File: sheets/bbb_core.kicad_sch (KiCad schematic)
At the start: 11 parts, among them P10 BeagleBone_Black_Header, P11 BeagleBone_Black_Header, SW2 SW_DIP_x02, U2 CAT24C256

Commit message: push
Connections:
- net GPIO117 renamed SPI0.CS3
- net GPIO2 renamed SPI0.SCLK
- net GPIO3 renamed SPI0.D0
- net GPIO4 renamed SPI0.CS0
- net GPIO48 renamed SPI0.CS1
- net GPIO49 renamed SPI0.CS2
- net GPIO5 renamed SPI0.D1

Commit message: pushing storage
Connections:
- net GPIO65 renamed MMC1.RST
- net MMC1.DAT3 renamed MCC1.DAT3
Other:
- moved on the sheet: P11

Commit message: push
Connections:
- net GPIO122 renamed SPI1.D1
- net GPIO14 renamed UART1_RXD
- net GPIO15 renamed UART1_TXD
- net GPIO26 renamed SPI1.CS8
- net GPIO44 renamed SPI1.CS7
- net GPIO45 renamed SPI1.CS3
- net GPIO47 renamed SPI1.CS4
- net GPIO66 renamed SPI1.CS1
- net GPIO67 renamed SPI1.CS5
- net GPIO68 renamed SPI1.CS6
- net GPIO69 renamed SPI1.CS2

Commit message: allocating pins ?
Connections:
- net GPIO22 renamed ACDS_GPIO_3
- net GPIO23 renamed ACDS_PWM_3
- net GPIO27 renamed ACDS_GPIO_2
- net GPIO40 renamed ACDS_PWM_1
- net GPIO51 renamed ACDS_PWM_2
- net GPIO60 renamed ACDS_GPIO_1
- net GPIO7 renamed HEATER_PWM
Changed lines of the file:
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@@
-		)
-	)
-	(label "GPIO27"
-		(at 187.96 53.34 0)
-		(effects
-			(font
-				(size 1.27 1.27)
-			)
-			(justify left bottom)
 		)
 	)
@@
 		)
 	)
-	(label "I2C2.SDA"
-		(at 135.89 55.88 180)
-		(effects
-			(font
-				(size 1.27 1.27)
-			)
-			(justify right bottom)
-		)
-	)
 	(label "LCD.DATA8"
 		(at 187.96 78.74 0)
@@
 		)
 	)
-	(label "GPIO51"
-		(at 135.89 50.8 180)
-		(effects
-			(font
-				(size 1.27 1.27)
-			)
-			(justify right bottom)
-		)
-	)
 	(label "LCD.AC_BIAS_E"
 		(at 238.76 68.58 180)
@@
 		)
 	)
-	(label "GPIO40"
-		(at 135.89 48.26 180)
-		(effects
-			(font
-				(size 1.27 1.27)
-			)
-			(justify right bottom)
-		)
-	)
 	(label "PWR_BUT"
 		(at 85.09 43.18 0)
@@
 		)
 	)
-	(label "GPIO60"
-		(at 135.89 45.72 180)
-		(effects
-			(font
-				(size 1.27 1.27)
-			)
-			(justify right bottom)
-		)
-	)
 	(label "I2C2.SDA"
 		(at 161.29 119.38 180)
@@
 			)
 			(justify right bottom)
-		)
-	)
-	(label "GPIO23"
-		(at 187.96 48.26 0)
-		(effects
-			(font
-				(size 1.27 1.27)
-			)
-			(justify left bottom)
-		)
-	)
-	(label "GPIO7"
-		(at 135.89 83.82 180)
-		(effects
-			(font
-				(size 1.27 1.27)
-			)
-			(justify right bottom)
-		)
-	)
-	(label "I2C2.SCL"
-		(at 85.09 55.88 0)
-		(effects
-			(font
-				(size 1.27 1.27)
-			)
-			(justify left bottom)
-		)
-	)
-	(label "GPIO22"
-		(at 187.96 55.88 0)
-		(effects
-			(font
-				(size 1.27 1.27)
-			)
-			(justify left bottom)
 		)
 	)
@@
 		)
 	)
+	(global_label "HEATER_PWM"
+		(shape output)
+		(at 135.89 83.82 0)
+		(fields_autoplaced yes)
+		(effects
+			(font
+				(size 1.27 1.27)
+			)
+			(justify left)
+		)
+		(property "Intersheetrefs" "${INTERSHEET_REFS}"
+			(at 151.0654 83.82 0)
+			(hide yes)
+			(show_name no)
+			(do_not_autoplace no)
+			(effects
+				(font
+					(size 1.27 1.27)
+				)
+				(justify left)
+			)
+		)
+	)
+	(global_label "ACDS_PWM_1"
+		(shape output)
+		(at 135.89 48.26 0)
+		(fields_autoplaced yes)
+		(effects
+			(font
+				(size 1.27 1.27)
+			)
+			(justify left)
+		)
+		(property "Intersheetrefs" "${INTERSHEET_REFS}"
+			(at 151.1259 48.26 0)
+			(hide yes)
+			(show_name no)
+			(do_not_autoplace no)
+			(effects
+				(font
+					(size 1.27 1.27)
+				)
+				(justify left)
+			)
+		)
+	)
 	(global_label "SPI1.D1"
 		(shape output)
@@
 		)
 	)
+	(global_label "ACDS_GPIO_2"
+		(shape output)
+		(at 187.96 53.34 180)
+		(fields_autoplaced yes)
+		(effects
+			(font
+				(size 1.27 1.27)
+			)
+			(justify right)
+		)
+		(property "Intersheetrefs" "${INTERSHEET_REFS}"
+			(at 172.4216 53.34 0)
+			(hide yes)
+			(show_name no)
+			(do_not_autoplace no)
+			(effects
+				(font
+					(size 1.27 1.27)
+				)
+				(justify right)
+			)
+		)
+	)
 	(global_label "SPI1.CS7"
 		(shape output)
@@
 		(property "Intersheetrefs" "${INTERSHEET_REFS}"
 			(at 250.4279 45.72 0)
+			(hide yes)
+			(show_name no)
+			(do_not_autoplace no)
+			(effects
+				(font
+					(size 1.27 1.27)
+				)
+				(justify left)
+			)
+		)
+	)
+	(global_label "ACDS_GPIO_1"
+		(shape output)
+		(at 135.89 45.72 0)
+		(fields_autoplaced yes)
+		(effects
+			(font
+				(size 1.27 1.27)
+			)
+			(justify left)
+		)
+		(property "Intersheetrefs" "${INTERSHEET_REFS}"
+			(at 151.4284 45.72 0)
 			(hide yes)
 			(show_name no)
@@
 		)
 	)
+	(global_label "ACDS_GPIO_3"
+		(shape output)
+		(at 187.96 55.88 180)
+		(fields_autoplaced yes)
+		(effects
+			(font
+				(size 1.27 1.27)
+			)
+			(justify right)
+		)
+		(property "Intersheetrefs" "${INTERSHEET_REFS}"
+			(at 172.4216 55.88 0)
+			(hide yes)
+			(show_name no)
+			(do_not_autoplace no)
+			(effects
+				(font
+					(size 1.27 1.27)
+				)
+				(justify right)
+			)
+		)
+	)
 	(global_label "SPI1.CS0"
 		(shape output)
@@
 		)
 	)
+	(global_label "ACDS_PWM_2"
+		(shape output)
+		(at 135.89 50.8 0)
+		(fields_autoplaced yes)
+		(effects
+			(font
+				(size 1.27 1.27)
+			)
+			(justify left)
+		)
+		(property "Intersheetrefs" "${INTERSHEET_REFS}"
+			(at 151.1259 50.8 0)
+			(hide yes)
+			(show_name no)
+			(do_not_autoplace no)
+			(effects
+				(font
+					(size 1.27 1.27)
+				)
+				(justify left)
+			)
+		)
+	)
 	(global_label "MMC1.CLK"
 		(shape output)
@@
 		)
 	)
+	(global_label "ACDS_PWM_3"
+		(shape output)
+		(at 187.96 48.26 180)
+		(fields_autoplaced yes)
+		(effects
+			(font
+				(size 1.27 1.27)
+			)
+			(justify right)
+		)
+		(property "Intersheetrefs" "${INTERSHEET_REFS}"
+			(at 172.7241 48.26 0)
+			(hide yes)
+			(show_name no)
+			(do_not_autoplace no)
+			(effects
+				(font
+					(size 1.27 1.27)
+				)
+				(justify right)
+			)
+		)
+	)
 	(global_label "SPI0.CS1"
 		(shape output)
@@
 			)
 		)
+	)
+	(global_label "I2C2.SCL"
+		(shape output)
+		(at 85.09 55.88 180)
+		(fields_autoplaced yes)
+		(effects
+			(font
+				(size 1.27 1.27)
+			)
+			(justify right)
+		)
+		(property "Intersheetrefs" "${INTERSHEET_REFS}"
+			(at 73.6035 55.88 0)
+			(hide yes)
+			(show_name no)
+			(do_not_autoplace no)
+			(effects
+				(font
+					(size 1.27 1.27)
+				)
+				(justify right)
+			)
+		)
+	)
+	(global_label "I2C2.SDA"
+		(shape output)
+		(at 135.89 55.88 0)
+		(fields_autoplaced yes)
+		(effects
+			(font
+				(size 1.27 1.27)
+			)
+			(justify left)
+		)
+		(property "Intersheetrefs" "${INTERSHEET_REFS}"
+			(at 147.437 55.88 0)
+			(hide yes)
+			(show_name no)
+			(do_not_autoplace no)
+			(effects
+				(font
+					(size 1.27 1.27)
+				)
+				(justify left)
+			)
+		)

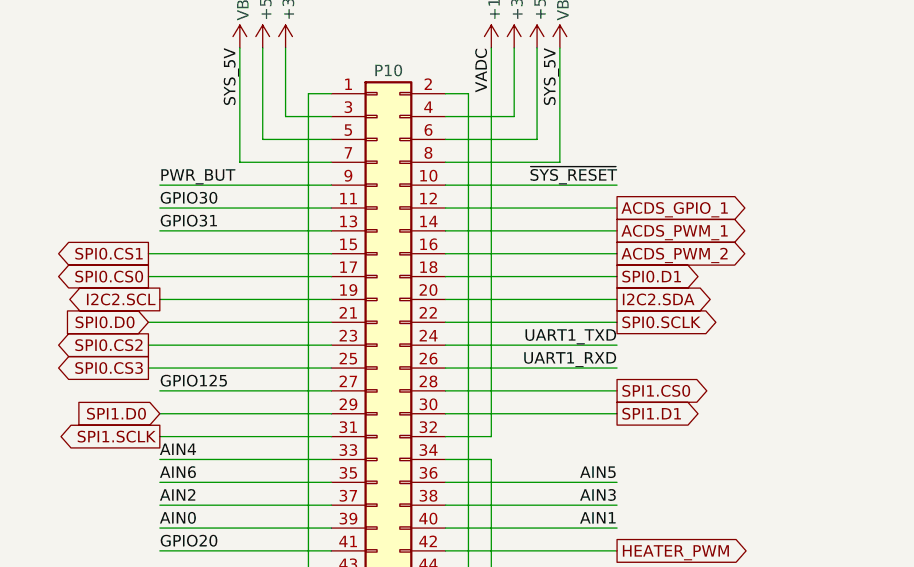
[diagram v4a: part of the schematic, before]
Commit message: uart global labels (not mapped onto pc104 yet)
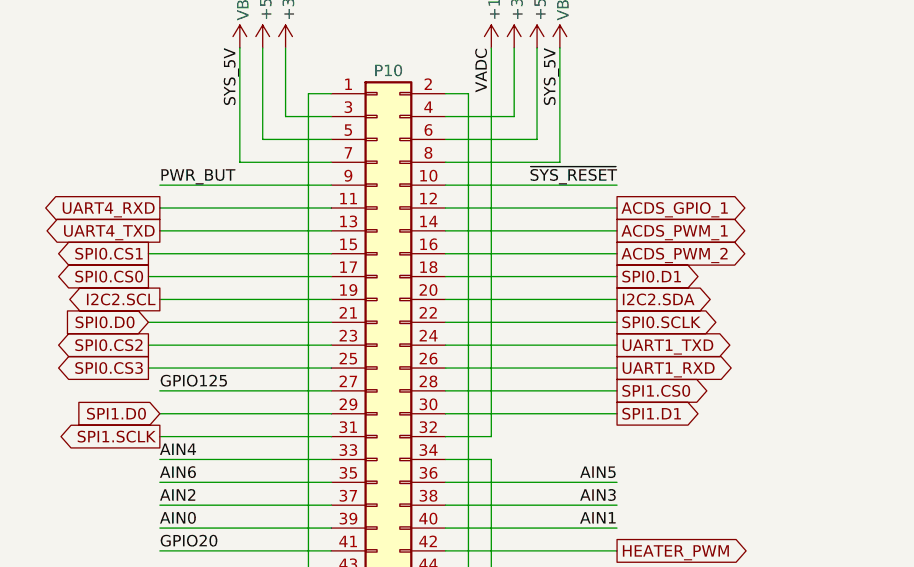
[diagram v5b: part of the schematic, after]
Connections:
- net GPIO30 renamed UART4_RXD
- net GPIO31 renamed UART4_TXD
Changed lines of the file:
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@@
-		)
-	)
-	(label "GPIO30"
-		(at 85.09 45.72 0)
-		(effects
-			(font
-				(size 1.27 1.27)
-			)
-			(justify left bottom)
 		)
 	)
@@
 		)
 	)
-	(label "GPIO31"
-		(at 85.09 48.26 0)
-		(effects
-			(font
-				(size 1.27 1.27)
-			)
-			(justify left bottom)
-		)
-	)
-	(label "UART1_RXD"
-		(at 135.89 63.5 180)
-		(effects
-			(font
-				(size 1.27 1.27)
-			)
-			(justify right bottom)
-		)
-	)
 	(label "GPIO61"
 		(at 238.76 66.04 180)
@@
 	(label "LCD.DATA5"
 		(at 238.76 83.82 180)
-		(effects
-			(font
-				(size 1.27 1.27)
-			)
-			(justify right bottom)
-		)
-	)
-	(label "UART1_TXD"
-		(at 135.89 60.96 180)
 		(effects
 			(font
@@
 		)
 	)
+	(global_label "UART4_RXD"
+		(shape output)
+		(at 85.09 45.72 180)
+		(fields_autoplaced yes)
+		(effects
+			(font
+				(size 1.27 1.27)
+			)
+			(justify right)
+		)
+		(property "Intersheetrefs" "${INTERSHEET_REFS}"
+			(at 71.4264 45.72 0)
+			(hide yes)
+			(show_name no)
+			(do_not_autoplace no)
+			(effects
+				(font
+					(size 1.27 1.27)
+				)
+				(justify right)
+			)
+		)
+	)
 	(global_label "SPI1.CS2"
 		(shape output)
@@
 		(property "Intersheetrefs" "${INTERSHEET_REFS}"
 			(at 176.2921 40.64 0)
+			(hide yes)
+			(show_name no)
+			(do_not_autoplace no)
+			(effects
+				(font
+					(size 1.27 1.27)
+				)
+				(justify right)
+			)
+		)
+	)
+	(global_label "UART4_TXD"
+		(shape output)
+		(at 85.09 48.26 180)
+		(fields_autoplaced yes)
+		(effects
+			(font
+				(size 1.27 1.27)
+			)
+			(justify right)
+		)
+		(property "Intersheetrefs" "${INTERSHEET_REFS}"
+			(at 71.7288 48.26 0)
 			(hide yes)
 			(show_name no)
@@
 			(hide yes)
 			(show_name no)
+			(do_not_autoplace no)
+			(effects
+				(font
+					(size 1.27 1.27)
+				)
+				(justify left)
+			)
+		)
+	)
+	(global_label "UART1_TXD"
+		(shape output)
+		(at 135.89 60.96 0)
+		(fields_autoplaced yes)
+		(effects
+			(font
+				(size 1.27 1.27)
+			)
+			(justify left)
+		)
+		(property "Intersheetrefs" "${INTERSHEET_REFS}"
+			(at 149.2512 60.96 0)
+			(hide yes)
+			(show_name no)
+			(do_not_autoplace no)
+			(effects
+				(font
+					(size 1.27 1.27)
+				)
+				(justify left)
+			)
+		)
+	)
+	(global_label "UART1_RXD"
+		(shape output)
+		(at 135.89 63.5 0)
+		(fields_autoplaced yes)
+		(effects
+			(font
+				(size 1.27 1.27)
+			)
+			(justify left)
+		)
+		(property "Intersheetrefs" "${INTERSHEET_REFS}"
+			(at 149.5536 63.5 0)
+			(hide yes)
+			(show_name no)

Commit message: one more uart (I think it is needed)
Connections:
- net LCD.DATA9 is gone; now on net UART1_RXD: P11.38 (Pin_38)
- net LCD.DATA8 renamed UART5_TXD
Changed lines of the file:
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@@
-		)
-	)
-	(label "LCD.DATA8"
-		(at 187.96 78.74 0)
-		(effects
-			(font
-				(size 1.27 1.27)
-			)
-			(justify left bottom)
 		)
 	)
@@
 	(label "AIN3"
 		(at 135.89 78.74 180)
-		(effects
-			(font
-				(size 1.27 1.27)
-			)
-			(justify right bottom)
-		)
-	)
-	(label "LCD.DATA9"
-		(at 238.76 78.74 180)
 		(effects
 			(font
@@
 	)
 	(global_label "UART4_RXD"
-		(shape output)
+		(shape input)
 		(at 85.09 45.72 180)
 		(fields_autoplaced yes)
@@
 		)
 	)
+	(global_label "UART1_RXD"
+		(shape input)
+		(at 238.76 78.74 0)
+		(fields_autoplaced yes)
+		(effects
+			(font
+				(size 1.27 1.27)
+			)
+			(justify left)
+		)
+		(property "Intersheetrefs" "${INTERSHEET_REFS}"
+			(at 252.4236 78.74 0)
+			(hide yes)
+			(show_name no)
+			(do_not_autoplace no)
+			(effects
+				(font
+					(size 1.27 1.27)
+				)
+				(justify left)
+			)
+		)
+	)
 	(global_label "UART1_TXD"
 		(shape output)
@@
 		)
 	)
+	(global_label "UART5_TXD"
+		(shape output)
+		(at 187.96 78.74 180)
+		(fields_autoplaced yes)
+		(effects
+			(font
+				(size 1.27 1.27)
+			)
+			(justify right)
+		)
+		(property "Intersheetrefs" "${INTERSHEET_REFS}"
+			(at 174.5988 78.74 0)
+			(hide yes)
+			(show_name no)
+			(do_not_autoplace no)
+			(effects
+				(font
+					(size 1.27 1.27)
+				)
+				(justify right)
+			)
+		)
+	)
 	(global_label "UART1_RXD"
-		(shape output)
+		(shape input)
 		(at 135.89 63.5 0)
 		(fields_autoplaced yes)

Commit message: Update bbb_core.kicad_sch
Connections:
- net UART1_RXD: no longer P11.38 (Pin_38)
- new net UART5_RXD: P11.38 (Pin_38)
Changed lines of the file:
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@@
 		)
 	)
-	(global_label "UART1_RXD"
+	(global_label "UART5_RXD"
 		(shape input)
 		(at 238.76 78.74 0)
